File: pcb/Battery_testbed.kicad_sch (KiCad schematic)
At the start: 13 parts, among them U6 MCP73831-2-OT, U7 MIC5504-3.3YM5

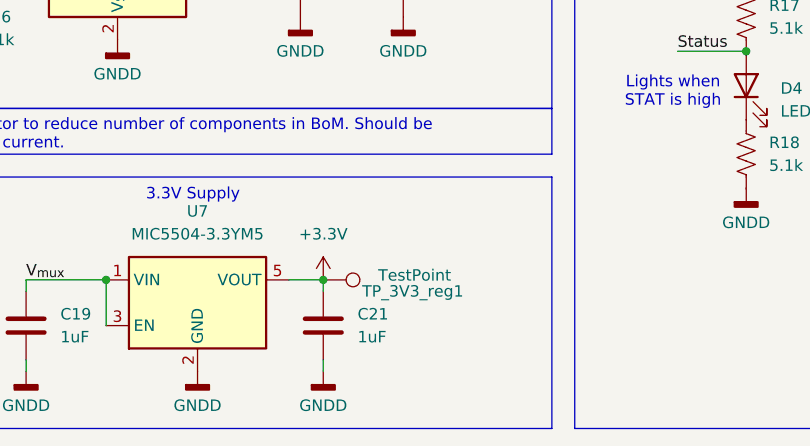
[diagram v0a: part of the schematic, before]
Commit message: Updated schematics and removed most test points
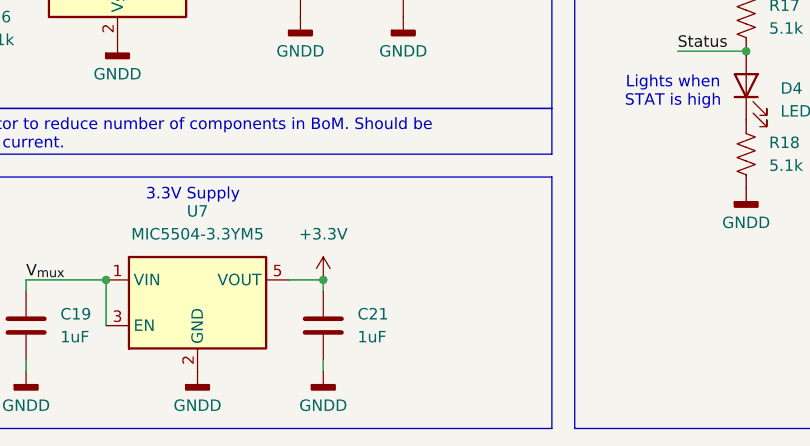
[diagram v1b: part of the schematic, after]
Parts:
- removed TP_3V3_reg1: TestPoint, TestPoint:TestPoint_Loop_D2.54mm_Drill1.5mm_Beaded, symbol Connector:TestPoint
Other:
- company: Dynamite Rocketry -> Rowan Rocketry
- title: Battery and Power -> Control Module Rev2
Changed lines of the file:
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@@
 	(generator "eeschema")
 	(generator_version "9.0")
-	(paper "A4")
+	(paper "USLetter")
 	(title_block
-		(title "Battery and Power")
-		(company "Dynamite Rocketry")
+		(title "Control Module Rev2")
+		(date "2026-02-10")
+		(rev "2.0")
+		(company "Rowan Rocketry")
 	)
 	(rectangle
@@
 		(dnp no)
 		(fields_autoplaced yes)
-		(property "Reference" "#PWR080"
+		(property "Reference" "#PWR077"
 			(at 106.68 134.62 0)
 			(effects
@@
 			(project "dyna-micro"
 				(path "/ba7b4294-8d75-4b9e-892f-fb52727887ec/5906240e-8ee4-4d86-a3fe-186c4ac07fa9"
-					(reference "#PWR080")
+					(reference "#PWR077")
 					(unit 1)
 				)
@@
 		(dnp no)
 		(fields_autoplaced yes)
-		(property "Reference" "#PWR083"
+		(property "Reference" "#PWR080"
 			(at 137.16 95.25 0)
 			(effects
@@
 			(project "dyna-micro"
 				(path "/ba7b4294-8d75-4b9e-892f-fb52727887ec/5906240e-8ee4-4d86-a3fe-186c4ac07fa9"
-					(reference "#PWR083")
+					(reference "#PWR080")
 					(unit 1)
 				)
@@
 		(dnp no)
 		(fields_autoplaced yes)
-		(property "Reference" "#PWR087"
+		(property "Reference" "#PWR084"
 			(at 186.69 81.28 0)
 			(effects
@@
 			(project "control-module"
 				(path "/ba7b4294-8d75-4b9e-892f-fb52727887ec/5906240e-8ee4-4d86-a3fe-186c4ac07fa9"
-					(reference "#PWR087")
+					(reference "#PWR084")
 					(unit 1)
 				)
@@
 		(dnp no)
 		(fields_autoplaced yes)
-		(property "Reference" "#PWR086"
+		(property "Reference" "#PWR083"
 			(at 148.59 95.25 0)
 			(effects
@@
 			(project "dyna-micro"
 				(path "/ba7b4294-8d75-4b9e-892f-fb52727887ec/5906240e-8ee4-4d86-a3fe-186c4ac07fa9"
-					(reference "#PWR086")
+					(reference "#PWR083")
 					(unit 1)
 				)
@@
 		(dnp no)
 		(fields_autoplaced yes)
-		(property "Reference" "#PWR079"
+		(property "Reference" "#PWR076"
 			(at 99.06 100.33 0)
 			(effects
@@
 			(project ""
 				(path "/ba7b4294-8d75-4b9e-892f-fb52727887ec/5906240e-8ee4-4d86-a3fe-186c4ac07fa9"
-					(reference "#PWR079")
+					(reference "#PWR076")
 					(unit 1)
 				)
@@
 		(dnp no)
 		(fields_autoplaced yes)
-		(property "Reference" "#PWR082"
+		(property "Reference" "#PWR079"
 			(at 125.73 134.62 0)
 			(effects
@@
 			(project "dyna-micro"
 				(path "/ba7b4294-8d75-4b9e-892f-fb52727887ec/5906240e-8ee4-4d86-a3fe-186c4ac07fa9"
-					(reference "#PWR082")
+					(reference "#PWR079")
 					(unit 1)
 				)
@@
 		(dnp no)
 		(fields_autoplaced yes)
-		(property "Reference" "#PWR085"
+		(property "Reference" "#PWR082"
 			(at 139.7 134.62 0)
 			(effects
@@
 			(project "dyna-micro"
 				(path "/ba7b4294-8d75-4b9e-892f-fb52727887ec/5906240e-8ee4-4d86-a3fe-186c4ac07fa9"
-					(reference "#PWR085")
+					(reference "#PWR082")
 					(unit 1)
 				)
@@
 		(dnp no)
 		(fields_autoplaced yes)
-		(property "Reference" "#PWR084"
+		(property "Reference" "#PWR081"
 			(at 139.7 121.92 0)
 			(effects
@@
 			(project ""
 				(path "/ba7b4294-8d75-4b9e-892f-fb52727887ec/5906240e-8ee4-4d86-a3fe-186c4ac07fa9"
-					(reference "#PWR084")
+					(reference "#PWR081")
 					(unit 1)
 				)
@@
 		(dnp no)
 		(fields_autoplaced yes)
-		(property "Reference" "#PWR077"
+		(property "Reference" "#PWR074"
 			(at 87.63 85.09 0)
 			(effects
@@
 			(project "control-module"
 				(path "/ba7b4294-8d75-4b9e-892f-fb52727887ec/5906240e-8ee4-4d86-a3fe-186c4ac07fa9"
-					(reference "#PWR077")
+					(reference "#PWR074")
 					(unit 1)
 				)
@@
 	)
 	(symbol
-		(lib_id "Connector:TestPoint")
-		(at 139.7 118.11 270)
-		(unit 1)
-		(exclude_from_sim no)
-		(in_bom yes)
-		(on_board yes)
-		(dnp no)
-		(property "Reference" "TP_3V3_reg1"
-			(at 144.018 119.38 90)
-			(effects
-				(font
-					(size 1.27 1.27)
-				)
-				(justify left)
-			)
-		)
-		(property "Value" "TestPoint"
-			(at 145.796 117.602 90)
-			(effects
-				(font
-					(size 1.27 1.27)
-				)
-				(justify left)
-			)
-		)
-		(property "Footprint" "TestPoint:TestPoint_Loop_D2.54mm_Drill1.5mm_Beaded"
-			(at 139.7 123.19 0)
-			(effects
-				(font
-					(size 1.27 1.27)
-				)
-				(hide yes)
-			)
-		)
-		(property "Datasheet" "https://www.keyelco.com/userAssets/file/M65p56.pdf"
-			(at 139.7 123.19 0)
-			(effects
-				(font
-					(size 1.27 1.27)
-				)
-				(hide yes)
-			)
-		)
-		(property "Description" "test point"
-			(at 139.7 118.11 0)
-			(effects
-				(font
-					(size 1.27 1.27)
-				)
-				(hide yes)
-			)
-		)
-		(property "Purchase" "https://www.digikey.com/en/products/detail/keystone-electronics/5000/255326"
-			(at 139.7 118.11 0)
-			(effects
-				(font
-					(size 1.27 1.27)
-				)
-				(hide yes)
-			)
-		)
-		(pin "1"
-		)
-		(instances
-			(project "control-module"
-				(path "/ba7b4294-8d75-4b9e-892f-fb52727887ec/5906240e-8ee4-4d86-a3fe-186c4ac07fa9"
-					(reference "TP_3V3_reg1")
-					(unit 1)
-				)
-			)
-		)
-	)
-	(symbol
 		(lib_id "power:GNDD")
 		(at 87.63 88.9 0)
@@
 		(dnp no)
 		(fields_autoplaced yes)
-		(property "Reference" "#PWR078"
+		(property "Reference" "#PWR075"
 			(at 87.63 95.25 0)
 			(effects
@@
 			(project "dyna-micro"
 				(path "/ba7b4294-8d75-4b9e-892f-fb52727887ec/5906240e-8ee4-4d86-a3fe-186c4ac07fa9"
-					(reference "#PWR078")
+					(reference "#PWR075")
 					(unit 1)
 				)
@@
 		(dnp no)
 		(fields_autoplaced yes)
-		(property "Reference" "#PWR088"
+		(property "Reference" "#PWR085"
 			(at 186.69 114.3 0)
 			(effects
@@
 			(project ""
 				(path "/ba7b4294-8d75-4b9e-892f-fb52727887ec/5906240e-8ee4-4d86-a3fe-186c4ac07fa9"
-					(reference "#PWR088")
+					(reference "#PWR085")
 					(unit 1)
 				)
@@
 		(dnp no)
 		(fields_autoplaced yes)
-		(property "Reference" "#PWR081"
+		(property "Reference" "#PWR078"
 			(at 116.84 97.79 0)
 			(effects
@@
 			(project ""
 				(path "/ba7b4294-8d75-4b9e-892f-fb52727887ec/5906240e-8ee4-4d86-a3fe-186c4ac07fa9"
-					(reference "#PWR081")
-					(unit 1)
-				)
+					(reference "#PWR078")
+					(unit 1)
+				)

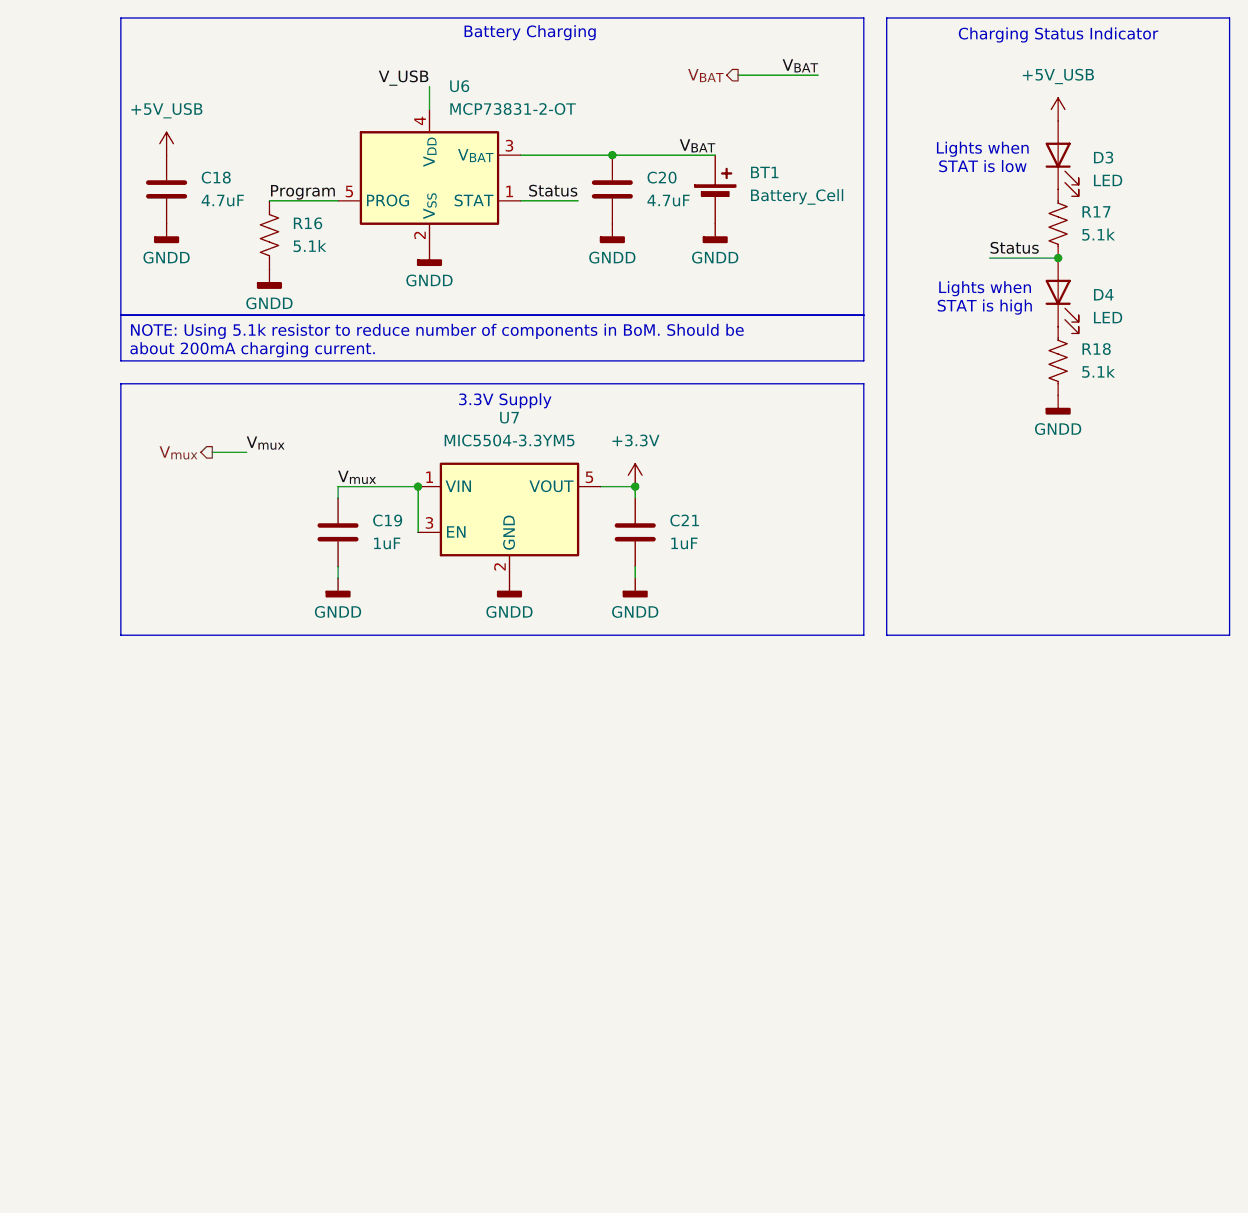
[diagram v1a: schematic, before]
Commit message: Updated Board size and layout
Full Layout of Rev 2 board, without RF shield and other updates.
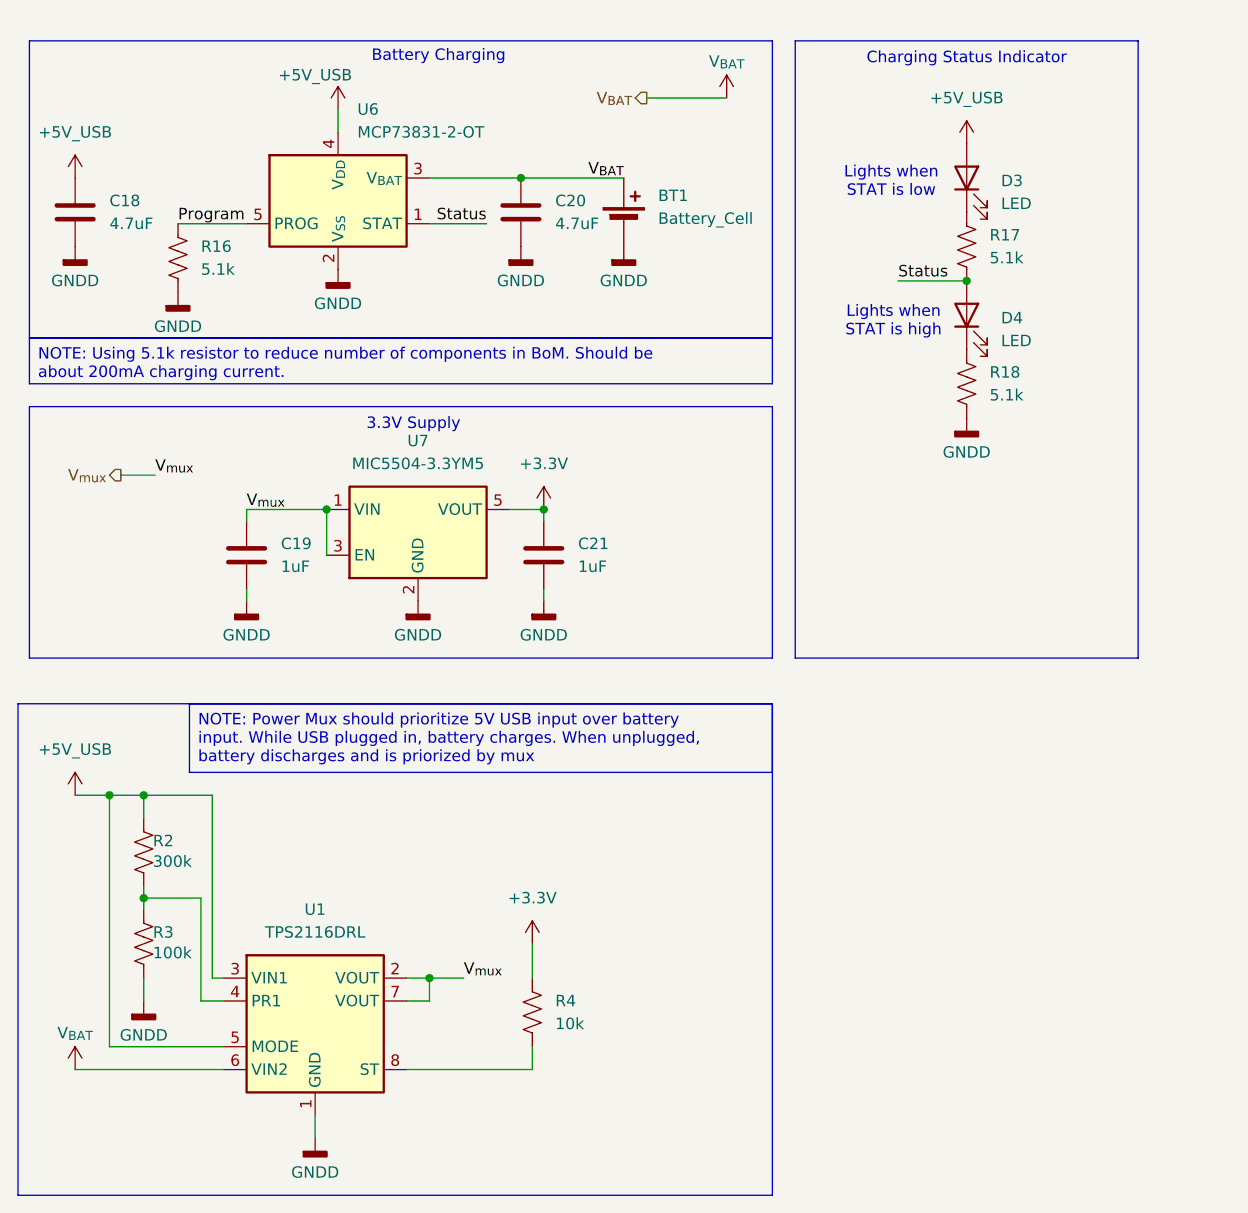
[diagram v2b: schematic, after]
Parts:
- added R2: 300k, Resistor_SMD:R_0603_1608Metric_Pad0.98x0.95mm_HandSolder, symbol Device:R_US
- added R3: 100k, Resistor_SMD:R_0603_1608Metric_Pad0.98x0.95mm_HandSolder, symbol Device:R_US
- added R4: 10k, Resistor_SMD:R_0603_1608Metric, symbol Device:R_US
- added U1: TPS2116DRL, Package_TO_SOT_SMD:SOT-583-8, symbol Power_Management:TPS2116DRL
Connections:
- net V_USB is gone; now on net +5V_USB: U6.4 (V_{DD})
- net +3.3V: now also R4.1
- net +5V_USB: now also R2.2, U1.3 (VIN1), U1.5 (MODE)
- net GNDD: now also R3.1, U1.1 (GND)
- net V_{BAT}: now also U1.6 (VIN2)
- net V_{mux}: now also U1.2 (VOUT), U1.7 (VOUT)
- new net: R2.1, R3.2, U1.4 (PR1)
- new net: R4.2, U1.8 (ST)
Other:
- moved on the sheet: BT1, C18, C19, C20, C21, D3, D4, R16, R17, R18, U6, U7
